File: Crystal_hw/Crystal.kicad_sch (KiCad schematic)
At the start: 71 parts, among them Q1 LED_5050, Q2 LED_5050, Q3 LED_5050, Q4 LED_5050, Q5 2N7002, SW1 BUTTON, SW2 BUTTON, SW3 BUTTON

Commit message: PCB is ready
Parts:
- removed SW1, SW2, SW3: BUTTON, BtnsSwitches:BTN_4x4_SMD, symbol BtnsSwitches:BUTTON
- added SA1: SS9, BtnsSwitches:SW_SS9, symbol BtnsSwitches:SWITCH_1P2T_housing
- added SW1, SW2, SW3: IT1198, BtnsSwitches:BTN_IT1198, symbol BtnsSwitches:BUTTON_H
- ANT1: footprint Antennas:Locket5 -> Antennas:Locket5_MIRR
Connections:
- net +3v3: now also SW1.2, SW2.1, SW3.1
- net +BATT: now also SA1.2; no longer XL3.2 (PM)
- net BTN_L: now also SW2.2
- net BTN_PWR: now also SW1.1
- net BTN_R: now also SW3.2
- net GND: now also SA1.H, SW1.H, SW2.H, SW3.H
- new net BAT2SW: SA1.1, XL3.2 (PM)
- no-connect marks 10 -> 11

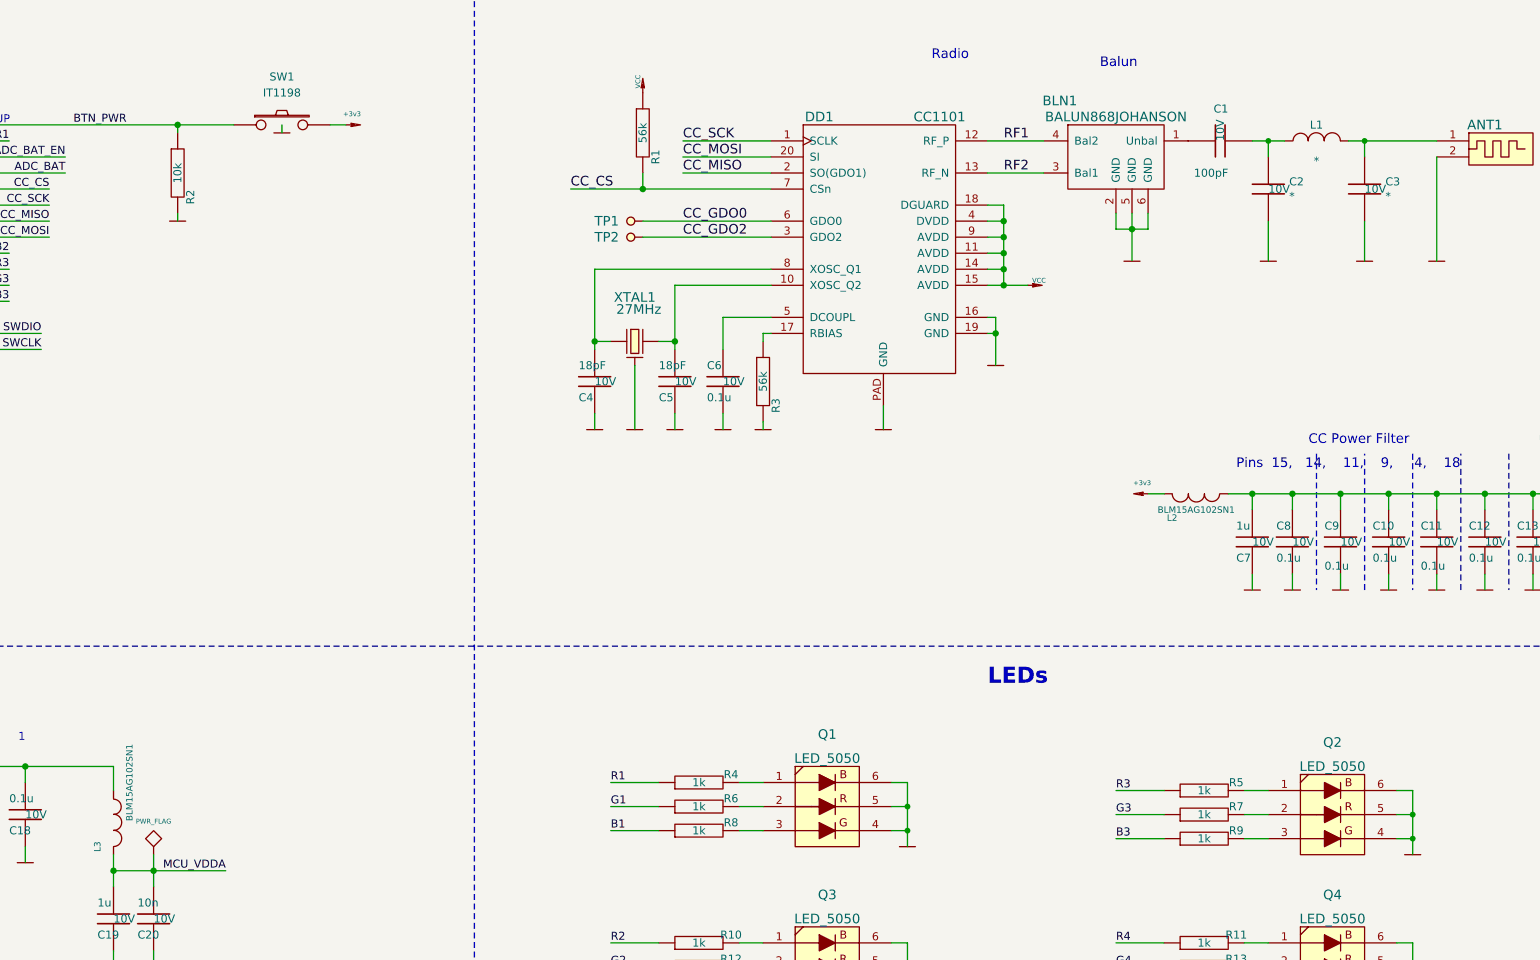
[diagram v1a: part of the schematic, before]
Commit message: + Antenna matched
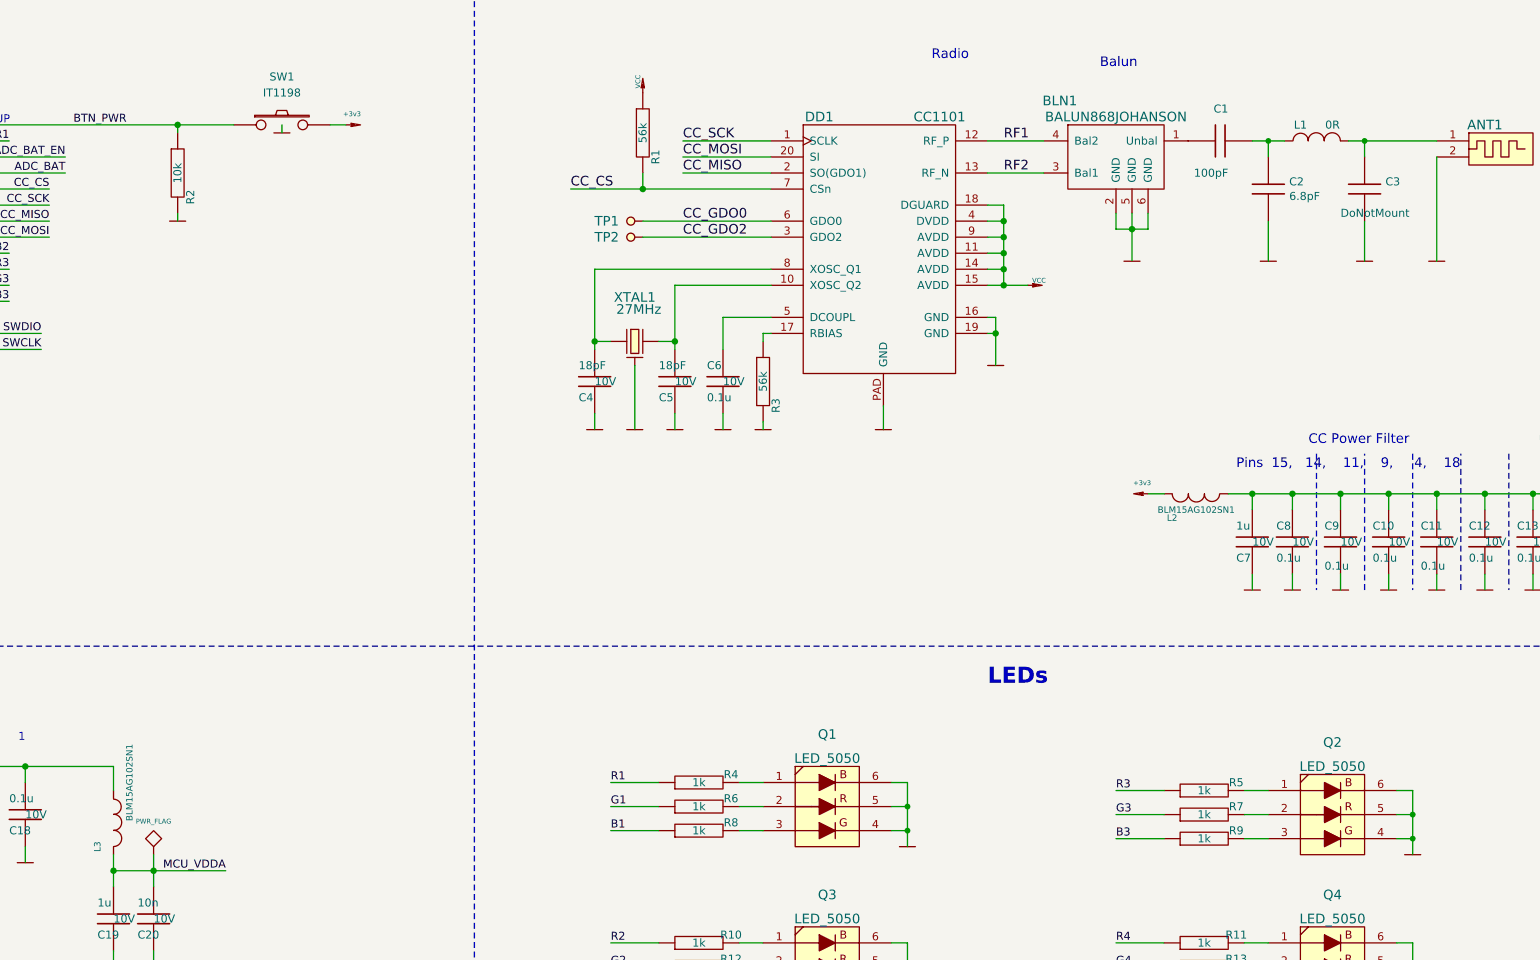
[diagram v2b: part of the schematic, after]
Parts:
- C1: Dielectric X5R or X7R -> NP0
- C2: value * -> 6.8pF; Dielectric X5R or X7R -> NP0
- C3: value * -> DoNotMount
- L1: value * -> 0R
